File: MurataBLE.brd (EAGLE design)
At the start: 92 x 70 mm, 46 parts, among them CON1 C-2235, IC1 I-5448, IC3 74LVC1G00DBV, Q1 FC-135 32.7680KA-AG3, Q2 12MHz, SW1 P8073, SW2 P8073, SW3 P8073, U1 IC_BLE_LBCA2HNZYZ-711, X1 TSW-114-02-S-S

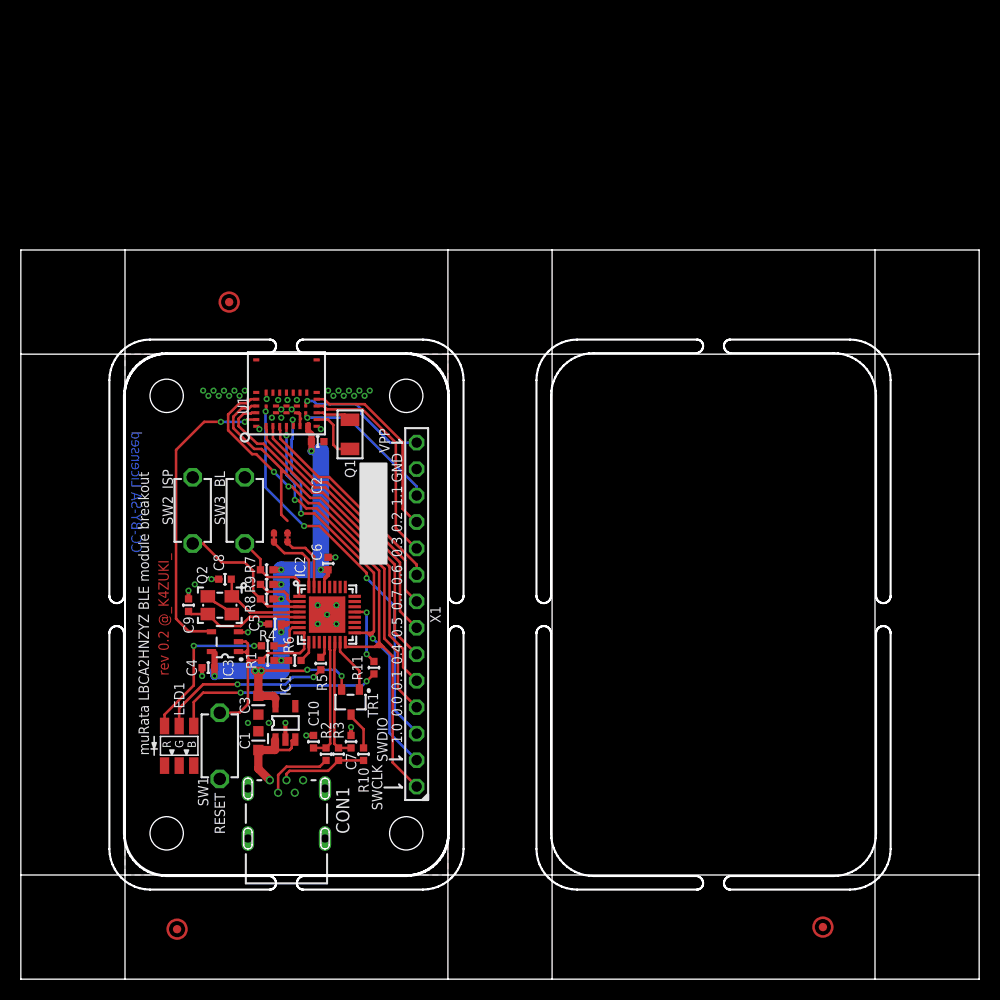
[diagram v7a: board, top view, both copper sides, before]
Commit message: [ USB ][ SCH ] test pads are connected
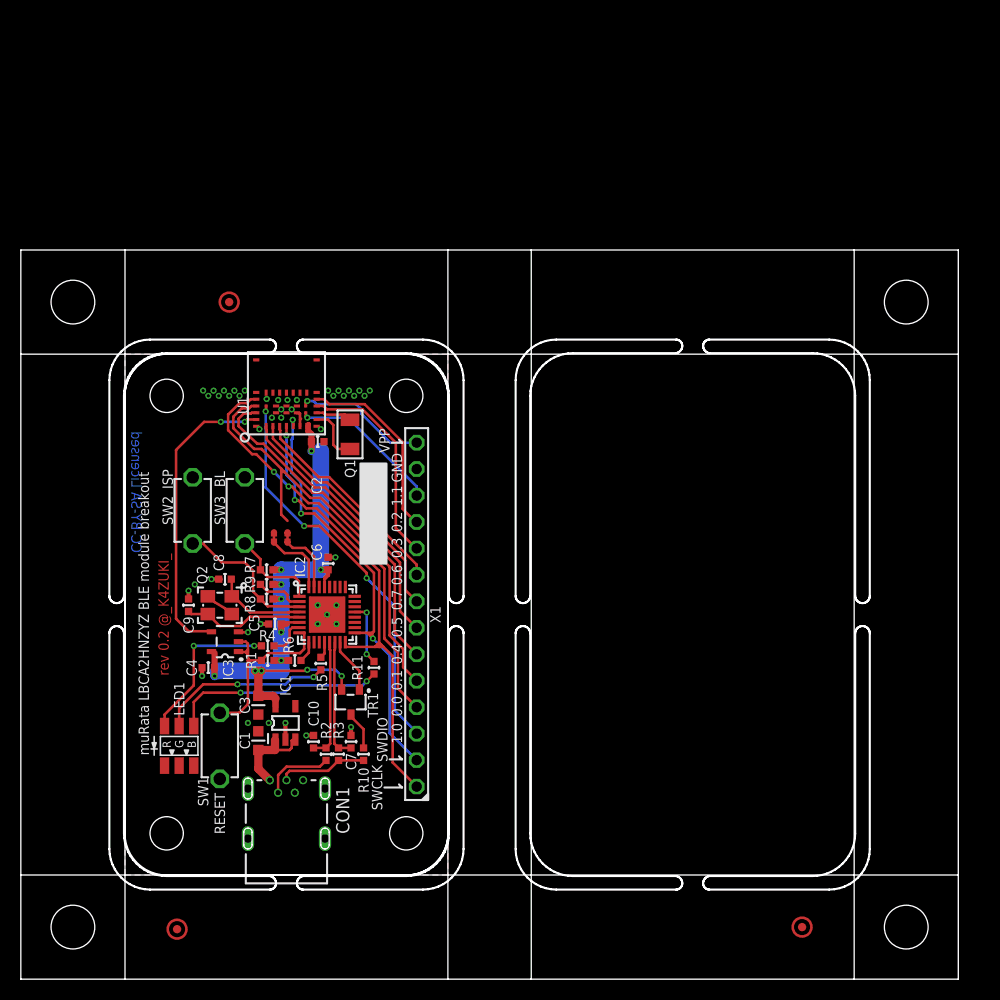
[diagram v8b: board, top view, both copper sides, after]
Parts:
- moved TP10 2.00 mm to (75.0, 5.00)
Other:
- board size 92 x 70 mm -> 90 x 70 mm
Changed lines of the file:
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@@
 <layer number="43" name="vRestrict" color="2" fill="10" visible="no" active="yes"/>
 <layer number="44" name="Drills" color="7" fill="1" visible="no" active="yes"/>
-<layer number="45" name="Holes" color="7" fill="1" visible="no" active="yes"/>
+<layer number="45" name="Holes" color="7" fill="1" visible="yes" active="yes"/>
 <layer number="46" name="Milling" color="3" fill="0" visible="yes" active="yes"/>
 <layer number="47" name="Measures" color="7" fill="1" visible="no" active="yes"/>
@@
 <text x="36.1" y="36.4" size="1" layer="21" ratio="20" rot="R90" align="center">0.7</text>
 <text x="36.1" y="38.8" size="1" layer="21" ratio="20" rot="R90" align="center">0.6</text>
-<text x="36.1" y="41.5" size="1" layer="21" ratio="20" rot="R90" align="center">0.3</text>
+<text x="36.1" y="41.4" size="1" layer="21" ratio="20" rot="R90" align="center">0.3</text>
 <text x="36.1" y="43.9" size="1" layer="21" ratio="20" rot="R90" align="center">0.2</text>
 <text x="36.1" y="49.1" size="1" layer="21" ratio="20" rot="R90" align="center">GND</text>
@@
 <wire x1="41" y1="70" x2="10" y2="70" width="0" layer="20"/>
 <wire x1="10" y1="0" x2="41" y2="0" width="0" layer="20"/>
-<wire x1="92" y1="0" x2="82" y2="0" width="0" layer="20"/>
-<wire x1="82" y1="0" x2="51" y2="0" width="0" layer="20"/>
-<wire x1="51" y1="0" x2="41" y2="0" width="0" layer="20"/>
-<wire x1="92" y1="70" x2="82" y2="70" width="0" layer="20"/>
-<wire x1="82" y1="70" x2="51" y2="70" width="0" layer="20"/>
-<wire x1="51" y1="70" x2="41" y2="70" width="0" layer="20"/>
-<wire x1="92" y1="70" x2="92" y2="60" width="0" layer="20"/>
-<dimension x1="0" y1="0" x2="92" y2="0" x3="46" y3="-3.4" textsize="1.778" textratio="20" layer="47" precision="3" visible="yes"/>
-<dimension x1="92" y1="0" x2="92" y2="70" x3="96.5" y3="35" textsize="1.778" textratio="20" layer="47" precision="3" visible="yes"/>
-<wire x1="92" y1="60" x2="92" y2="10" width="0" layer="20"/>
-<wire x1="92" y1="10" x2="92" y2="0" width="0" layer="20"/>
+<wire x1="90" y1="0" x2="80" y2="0" width="0" layer="20"/>
+<wire x1="80" y1="0" x2="49" y2="0" width="0" layer="20"/>
+<wire x1="49" y1="0" x2="41" y2="0" width="0" layer="20"/>
+<wire x1="90" y1="70" x2="80" y2="70" width="0" layer="20"/>
+<wire x1="80" y1="70" x2="49" y2="70" width="0" layer="20"/>
+<wire x1="49" y1="70" x2="41" y2="70" width="0" layer="20"/>
+<wire x1="90" y1="70" x2="90" y2="60" width="0" layer="20"/>
+<dimension x1="0" y1="0" x2="90" y2="0" x3="45" y3="-3.4" textsize="1.778" textratio="20" layer="47" precision="3" visible="yes"/>
+<dimension x1="90" y1="0" x2="90" y2="70" x3="94.5" y3="35" textsize="1.778" textratio="20" layer="47" precision="3" visible="yes"/>
+<wire x1="90" y1="60" x2="90" y2="10" width="0" layer="20"/>
+<wire x1="90" y1="10" x2="90" y2="0" width="0" layer="20"/>
 <text x="14.1" y="48" size="1" layer="21" ratio="20" rot="R90" align="center">ISP</text>
 <text x="19.1" y="48" size="1" layer="21" ratio="20" rot="R90" align="center">BL</text>
 <text x="19.1" y="15.9" size="1" layer="21" ratio="20" rot="R270" align="center">RESET</text>
-<wire x1="51" y1="70" x2="51" y2="0" width="0" layer="20"/>
+<wire x1="49" y1="70" x2="49" y2="0" width="0" layer="20"/>
 <wire x1="10" y1="70" x2="10" y2="0" width="0" layer="20"/>
-<wire x1="82" y1="70" x2="82" y2="0" width="0" layer="20"/>
+<wire x1="80" y1="70" x2="80" y2="0" width="0" layer="20"/>
 <circle x="35" y="66.5" radius="0.1" width="0.1" layer="52"/>
 <polygon width="0.2" layer="46">
@@
 </polygon>
 <polygon width="0.2" layer="46">
-<vertex x="50.9" y="36.8" curve="-90"/>
-<vertex x="50.2" y="36.1" curve="-90"/>
-<vertex x="49.5" y="36.8"/>
-<vertex x="49.5" y="57.5" curve="-90"/>
-<vertex x="53.4" y="61.4"/>
-<vertex x="64.9" y="61.4" curve="-90"/>
-<vertex x="65.5" y="60.8" curve="-81.202506"/>
-<vertex x="64.9" y="60.1"/>
-<vertex x="55" y="60.1" curve="90"/>
-<vertex x="50.9" y="56"/>
+<vertex x="48.9" y="36.8" curve="-90"/>
+<vertex x="48.2" y="36.1" curve="-90"/>
+<vertex x="47.5" y="36.8"/>
+<vertex x="47.5" y="57.5" curve="-90"/>
+<vertex x="51.4" y="61.4"/>
+<vertex x="62.9" y="61.4" curve="-90"/>
+<vertex x="63.5" y="60.8" curve="-81.202506"/>
+<vertex x="62.9" y="60.1"/>
+<vertex x="53" y="60.1" curve="90"/>
+<vertex x="48.9" y="56"/>
 </polygon>
 <polygon width="0.2" layer="46">
-<vertex x="50.9" y="33.2" curve="90"/>
-<vertex x="50.2" y="33.9" curve="90"/>
-<vertex x="49.5" y="33.2"/>
-<vertex x="49.5" y="12.5" curve="90"/>
-<vertex x="53.4" y="8.6"/>
-<vertex x="64.9" y="8.6" curve="90"/>
-<vertex x="65.5" y="9.2" curve="81.202506"/>
-<vertex x="64.9" y="9.9"/>
-<vertex x="55" y="9.9" curve="-90"/>
-<vertex x="50.9" y="14"/>
+<vertex x="48.9" y="33.2" curve="90"/>
+<vertex x="48.2" y="33.9" curve="90"/>
+<vertex x="47.5" y="33.2"/>
+<vertex x="47.5" y="12.5" curve="90"/>
+<vertex x="51.4" y="8.6"/>
+<vertex x="62.9" y="8.6" curve="90"/>
+<vertex x="63.5" y="9.2" curve="81.202506"/>
+<vertex x="62.9" y="9.9"/>
+<vertex x="53" y="9.9" curve="-90"/>
+<vertex x="48.9" y="14"/>
 </polygon>
 <polygon width="0.2" layer="46">
@@
 </polygon>
 <polygon width="0.2" layer="46">
-<vertex x="82.1" y="36.8" curve="90"/>
-<vertex x="82.8" y="36.1" curve="90"/>
-<vertex x="83.5" y="36.8"/>
-<vertex x="83.5" y="57.5" curve="90"/>
-<vertex x="79.6" y="61.4"/>
-<vertex x="68.1" y="61.4" curve="90"/>
-<vertex x="67.5" y="60.8" curve="81.202506"/>
-<vertex x="68.1" y="60.1"/>
-<vertex x="78" y="60.1" curve="-90"/>
-<vertex x="82.1" y="56"/>
+<vertex x="80.1" y="36.8" curve="90"/>
+<vertex x="80.8" y="36.1" curve="90"/>
+<vertex x="81.5" y="36.8"/>
+<vertex x="81.5" y="57.5" curve="90"/>
+<vertex x="77.6" y="61.4"/>
+<vertex x="66.1" y="61.4" curve="90"/>
+<vertex x="65.5" y="60.8" curve="81.202506"/>
+<vertex x="66.1" y="60.1"/>
+<vertex x="76" y="60.1" curve="-90"/>
+<vertex x="80.1" y="56"/>
 </polygon>
 <polygon width="0.2" layer="46">
-<vertex x="82.1" y="33.2" curve="-90"/>
-<vertex x="82.8" y="33.9" curve="-90"/>
-<vertex x="83.5" y="33.2"/>
-<vertex x="83.5" y="12.5" curve="-90"/>
-<vertex x="79.6" y="8.6"/>
-<vertex x="68.1" y="8.6" curve="-90"/>
-<vertex x="67.5" y="9.2" curve="-81.202506"/>
-<vertex x="68.1" y="9.9"/>
-<vertex x="78" y="9.9" curve="90"/>
-<vertex x="82.1" y="14"/>
-</polygon>
-<wire x1="0" y1="60" x2="92" y2="60" width="0" layer="20"/>
-<wire x1="0" y1="10" x2="92" y2="10" width="0" layer="20"/>
+<vertex x="80.1" y="33.2" curve="-90"/>
+<vertex x="80.8" y="33.9" curve="-90"/>
+<vertex x="81.5" y="33.2"/>
+<vertex x="81.5" y="12.5" curve="-90"/>
+<vertex x="77.6" y="8.6"/>
+<vertex x="66.1" y="8.6" curve="-90"/>
+<vertex x="65.5" y="9.2" curve="-81.202506"/>
+<vertex x="66.1" y="9.9"/>
+<vertex x="76" y="9.9" curve="90"/>
+<vertex x="80.1" y="14"/>
+</polygon>
+<wire x1="0" y1="60" x2="90" y2="60" width="0" layer="20"/>
+<wire x1="0" y1="10" x2="90" y2="10" width="0" layer="20"/>
 <wire x1="13.2" y1="19.7" x2="13.2" y2="21.4" width="0.25" layer="41"/>
 <wire x1="13.2" y1="21.4" x2="14.5" y2="21.4" width="0.25" layer="41"/>
@@
 <circle x="20" y="65" radius="0.9" width="0.25" layer="1"/>
 <circle x="15" y="4.8" radius="0.9" width="0.25" layer="1"/>
-<circle x="77" y="5" radius="0.9" width="0.25" layer="1"/>
+<circle x="75" y="5" radius="0.9" width="0.25" layer="1"/>
 <polygon width="0.25" layer="29">
-<vertex x="76.4" y="5" curve="-90"/>
-<vertex x="77" y="5.6" curve="-90"/>
-<vertex x="77.6" y="5" curve="-90"/>
-<vertex x="77" y="4.4" curve="-90"/>
+<vertex x="74.4" y="5" curve="-90"/>
+<vertex x="75" y="5.6" curve="-90"/>
+<vertex x="75.6" y="5" curve="-90"/>
+<vertex x="75" y="4.4" curve="-90"/>
 </polygon>
 <polygon width="0.25" layer="29">
@@
 <vertex x="20" y="64.4" curve="-90"/>
 </polygon>
+<hole x="5" y="65" drill="4.2"/>
+<hole x="5" y="5" drill="4.2"/>
+<hole x="85" y="5" drill="4.2"/>
+<hole x="85" y="65" drill="4.2"/>
 </plain>
 <attributes>
@@
 <attribute name="VALUE" x="14.619" y="4.292" size="0.0254" layer="27"/>
 </element>
-<element name="TP10" library="testpad_local" package="TP08R" value="TPTP08R" x="77" y="5" smashed="yes">
-<attribute name="TP_SIGNAL_NAME" value="" x="77" y="3.095" size="1" layer="37"/>
-<attribute name="VALUE" x="76.619" y="4.492" size="0.0254" layer="27"/>
+<element name="TP10" library="testpad_local" package="TP08R" value="TPTP08R" x="75" y="5" smashed="yes">
+<attribute name="TP_SIGNAL_NAME" value="" x="75" y="3.095" size="1" layer="37"/>
+<attribute name="VALUE" x="74.619" y="4.492" size="0.0254" layer="27"/>
 </element>
 <element name="TP11" library="testpad_local" package="TP08R" value="TPTP08R" x="20" y="65" smashed="yes">
